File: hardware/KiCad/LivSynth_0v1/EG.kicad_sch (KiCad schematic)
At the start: 28 parts, among them J5 Jumper, Q1 2N3904, Q2 2N3906, Q3 2N3906, Q4 2N3904, SW2 SW_SPST, U1 TL074

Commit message: Initial Routing finished
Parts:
- added D10: LED, LED_THT:LED_D5.0mm, symbol Device:LED
- R10: value 470 -> 360
- RV2, RV3: footprint (none) -> SloBlo:RV141F-40-20BL
- SW2: footprint (none) -> SloBlo:SW_Toggle_MS500C
- U5: renamed from U1; footprint (none) -> Package_SO:SOIC-14_3.9x8.7mm_P1.27mm
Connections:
- net AR_OUT: now also U5.1, U5.2 (-); no longer U5.8, U5.9 (-)
- net at R16.2, R18.1, R23.1: now also U5.5 (+); no longer U5.12 (+)
- net at C32.1, RV2.2, RV2.3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: now also U5.3 (+), U5.6 (-); no longer U5.10 (+), U5.13 (-)
- net at R18.2, SW2.2 (B): now also U5.7; no longer U5.14
- net at D2.2 (A): now also D10.1 (K); no longer R10.2
- net GATE_IN renamed GATE_OUT
- new net: D10.2 (A), R10.2
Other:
- note added: "R = (9-2*1.8)V/.015A = 360R"
- note removed: "R = (9-1.8)V/.015A ~= 470R"
- moved on the sheet: R10
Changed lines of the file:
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@@
+    (stroke (width 0) (type default) (color 0 0 0 0))
+  )
+  (wire (pts (xy 226.695 23.495) (xy 226.695 25.4))
+    (stroke (width 0) (type default) (color 0 0 0 0))
+  )
+  (wire (pts (xy 43.815 134.62) (xy 120.015 134.62))
+    (stroke (width 0) (type default) (color 0 0 0 0))
+  )
+  (wire (pts (xy 169.545 102.87) (xy 169.545 106.045))
+    (stroke (width 0) (type default) (color 0 0 0 0))
+  )
+  (wire (pts (xy 35.56 102.235) (xy 43.815 102.235))
+    (stroke (width 0) (type default) (color 0 0 0 0))
+  )
+  (wire (pts (xy 187.96 87.63) (xy 190.5 87.63))
+    (stroke (width 0) (type default) (color 0 0 0 0))
+  )
+  (wire (pts (xy 207.645 90.17) (xy 205.74 90.17))
+    (stroke (width 0) (type default) (color 0 0 0 0))
+  )
+  (wire (pts (xy 149.225 102.87) (xy 155.575 102.87))
+    (stroke (width 0) (type default) (color 0 0 0 0))
+  )
+  (wire (pts (xy 81.915 95.25) (xy 88.9 95.25))
+    (stroke (width 0) (type default) (color 0 0 0 0))
+  )
+  (wire (pts (xy 187.96 68.58) (xy 187.96 59.055))
+    (stroke (width 0) (type default) (color 0 0 0 0))
+  )
+  (wire (pts (xy 128.27 100.33) (xy 128.27 107.315))
     (stroke (width 0) (type default) (color 0 0 0 0))
   )
@@
     (stroke (width 0) (type default) (color 0 0 0 0))
   )
-  (wire (pts (xy 43.815 134.62) (xy 120.015 134.62))
-    (stroke (width 0) (type default) (color 0 0 0 0))
-  )
-  (wire (pts (xy 169.545 102.87) (xy 169.545 106.045))
-    (stroke (width 0) (type default) (color 0 0 0 0))
-  )
-  (wire (pts (xy 35.56 102.235) (xy 43.815 102.235))
-    (stroke (width 0) (type default) (color 0 0 0 0))
-  )
-  (wire (pts (xy 187.96 87.63) (xy 190.5 87.63))
-    (stroke (width 0) (type default) (color 0 0 0 0))
-  )
-  (wire (pts (xy 207.645 90.17) (xy 205.74 90.17))
-    (stroke (width 0) (type default) (color 0 0 0 0))
-  )
-  (wire (pts (xy 149.225 102.87) (xy 155.575 102.87))
-    (stroke (width 0) (type default) (color 0 0 0 0))
-  )
-  (wire (pts (xy 81.915 95.25) (xy 88.9 95.25))
-    (stroke (width 0) (type default) (color 0 0 0 0))
-  )
-  (wire (pts (xy 187.96 68.58) (xy 187.96 59.055))
-    (stroke (width 0) (type default) (color 0 0 0 0))
-  )
-  (wire (pts (xy 128.27 100.33) (xy 128.27 107.315))
-    (stroke (width 0) (type default) (color 0 0 0 0))
-  )
   (wire (pts (xy 163.195 87.63) (xy 164.465 87.63))
     (stroke (width 0) (type default) (color 0 0 0 0))
@@
     (stroke (width 0) (type default) (color 0 0 0 0))
   )
-  (text "R = (9-1.8)V/.015A ~= 470R" (at 237.49 38.735 0)
+  (text "R = (9-2*1.8)V/.015A = 360R" (at 237.49 38.735 0)
     (effects (font (size 1.27 1.27)) (justify left bottom))
   )
@@
     (effects (font (size 1.27 1.27)) (justify left bottom))
   )
-  (hierarchical_label "GATE_IN" (shape input) (at 26.035 102.235 180)
+  (hierarchical_label "GATE_OUT" (shape input) (at 26.035 102.235 180)
     (effects (font (size 1.27 1.27)) (justify right))
   )
@@
     (pin "1")
   )
-  (symbol (lib_id "Amplifier_Operational:TL074") (at 198.12 90.17 0) (mirror x) (unit 4)
+  (symbol (lib_id "Amplifier_Operational:TL074") (at 198.12 90.17 0) (mirror x) (unit 2)
     (in_bom yes) (on_board yes)
-    (property "Reference" "U1" (id 0) (at 198.12 82.55 0))
+    (property "Reference" "U5" (id 0) (at 198.12 82.55 0))
     (property "Value" "TL074" (id 1) (at 198.12 84.455 0))
-    (property "Footprint" "" (id 2) (at 196.85 92.71 0)
+    (property "Footprint" "Package_SO:SOIC-14_3.9x8.7mm_P1.27mm" (id 2) (at 196.85 92.71 0)
       (effects (font (size 1.27 1.27)) hide)
     )
@@
     (pin "2")
   )
-  (symbol (lib_id "Amplifier_Operational:TL074") (at 198.12 71.12 0) (mirror x) (unit 3)
+  (symbol (lib_id "Amplifier_Operational:TL074") (at 198.12 71.12 0) (mirror x) (unit 1)
     (in_bom yes) (on_board yes)
-    (property "Reference" "U1" (id 0) (at 198.12 63.5 0))
+    (property "Reference" "U5" (id 0) (at 198.12 63.5 0))
     (property "Value" "TL074" (id 1) (at 198.12 65.405 0))
-    (property "Footprint" "" (id 2) (at 196.85 73.66 0)
+    (property "Footprint" "Package_SO:SOIC-14_3.9x8.7mm_P1.27mm" (id 2) (at 196.85 73.66 0)
       (effects (font (size 1.27 1.27)) hide)
     )
@@
     (property "Reference" "RV2" (id 0) (at 159.385 90.805 90))
     (property "Value" "1M" (id 1) (at 159.385 93.345 90))
-    (property "Footprint" "" (id 2) (at 159.385 87.63 0)
+    (property "Footprint" "SloBlo:RV141F-40-20BL" (id 2) (at 159.385 87.63 0)
       (effects (font (size 1.27 1.27)) hide)
     )
@@
     (pin "1")
   )
+  (symbol (lib_id "Device:LED") (at 226.695 38.735 90) (unit 1)
+    (in_bom yes) (on_board yes) (fields_autoplaced)
+    (property "Reference" "D10" (id 0) (at 230.505 39.0524 90)
+      (effects (font (size 1.27 1.27)) (justify right))
+    )
+    (property "Value" "LED" (id 1) (at 230.505 41.5924 90)
+      (effects (font (size 1.27 1.27)) (justify right))
+    )
+    (property "Footprint" "LED_THT:LED_D5.0mm" (id 2) (at 226.695 38.735 0)
+      (effects (font (size 1.27 1.27)) hide)
+    )
+    (property "Datasheet" "~" (id 3) (at 226.695 38.735 0)
+      (effects (font (size 1.27 1.27)) hide)
+    )
+    (pin "1")
+    (pin "2")
+  )
   (symbol (lib_id "power:GND") (at 81.915 118.11 0) (unit 1)
     (in_bom yes) (on_board yes) (fields_autoplaced)
@@
     (pin "1")
   )
-  (symbol (lib_id "power:+9V") (at 226.695 33.02 0) (unit 1)
-    (in_bom yes) (on_board yes) (fields_autoplaced)
-    (property "Reference" "#PWR032" (id 0) (at 226.695 36.83 0)
-      (effects (font (size 1.27 1.27)) hide)
-    )
-    (property "Value" "+9V" (id 1) (at 226.695 27.305 0))
-    (property "Footprint" "" (id 2) (at 226.695 33.02 0)
-      (effects (font (size 1.27 1.27)) hide)
-    )
-    (property "Datasheet" "" (id 3) (at 226.695 33.02 0)
+  (symbol (lib_id "power:+9V") (at 226.695 23.495 0) (unit 1)
+    (in_bom yes) (on_board yes) (fields_autoplaced)
+    (property "Reference" "#PWR032" (id 0) (at 226.695 27.305 0)
+      (effects (font (size 1.27 1.27)) hide)
+    )
+    (property "Value" "+9V" (id 1) (at 226.695 17.78 0))
+    (property "Footprint" "" (id 2) (at 226.695 23.495 0)
+      (effects (font (size 1.27 1.27)) hide)
+    )
+    (property "Datasheet" "" (id 3) (at 226.695 23.495 0)
       (effects (font (size 1.27 1.27)) hide)
     )
@@
     (property "Reference" "RV3" (id 0) (at 159.385 106.045 90))
     (property "Value" "1M" (id 1) (at 159.385 108.585 90))
-    (property "Footprint" "" (id 2) (at 159.385 102.87 0)
+    (property "Footprint" "SloBlo:RV141F-40-20BL" (id 2) (at 159.385 102.87 0)
       (effects (font (size 1.27 1.27)) hide)
     )
@@
     (property "Reference" "SW2" (id 0) (at 125.095 128.27 0))
     (property "Value" "SW_SPST" (id 1) (at 125.095 130.81 0))
-    (property "Footprint" "" (id 2) (at 125.095 134.62 0)
+    (property "Footprint" "SloBlo:SW_Toggle_MS500C" (id 2) (at 125.095 134.62 0)
       (effects (font (size 1.27 1.27)) hide)
     )
@@
     (pin "2")
   )
-  (symbol (lib_id "Device:R") (at 226.695 38.735 0) (unit 1)
-    (in_bom yes) (on_board yes) (fields_autoplaced)
-    (property "Reference" "R10" (id 0) (at 228.6 37.4649 0)
-      (effects (font (size 1.27 1.27)) (justify left))
-    )
-    (property "Value" "470" (id 1) (at 228.6 40.0049 0)
-      (effects (font (size 1.27 1.27)) (justify left))
-    )
-    (property "Footprint" "Resistor_THT:R_Axial_DIN0207_L6.3mm_D2.5mm_P7.62mm_Horizontal" (id 2) (at 224.917 38.735 90)
-      (effects (font (size 1.27 1.27)) hide)
-    )
-    (property "Datasheet" "~" (id 3) (at 226.695 38.735 0)
-      (effects (font (size 1.27 1.27)) hide)
-    )
+  (symbol (lib_id "Device:R") (at 226.695 29.21 0) (unit 1)
+    (in_bom yes) (on_board yes) (fields_autoplaced)
+    (property "Reference" "R10" (id 0) (at 228.6 27.9399 0)
+      (effects (font (size 1.27 1.27)) (justify left))
+    )
+    (property "Value" "360" (id 1) (at 228.6 30.4799 0)
+      (effects (font (size 1.27 1.27)) (justify left))
+    )
+    (property "Footprint" "Resistor_THT:R_Axial_DIN0207_L6.3mm_D2.5mm_P7.62mm_Horizontal" (id 2) (at 224.917 29.21 90)
+      (effects (font (size 1.27 1.27)) hide)
+    )
+    (property "Datasheet" "~" (id 3) (at 226.695 29.21 0)
+      (effects (font (size 1.27 1.27)) hide)
+    )

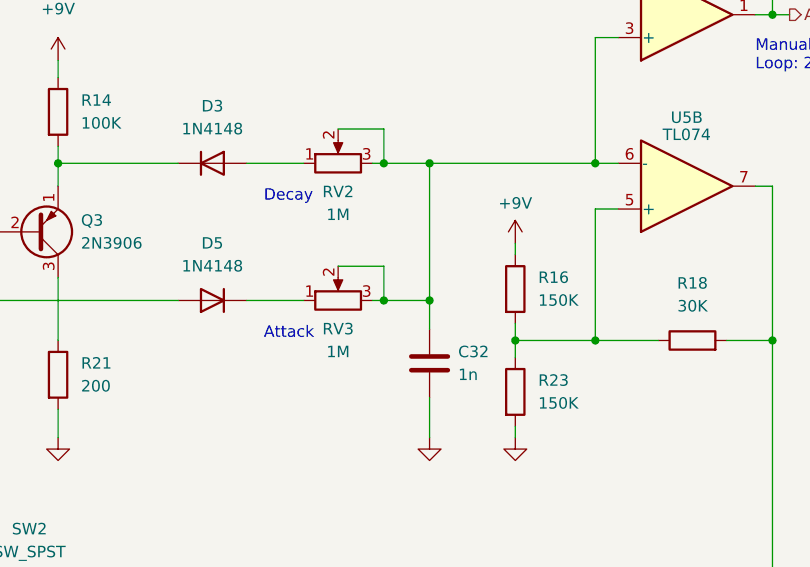
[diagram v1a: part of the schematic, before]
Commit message: Rework for polyester film capacitors
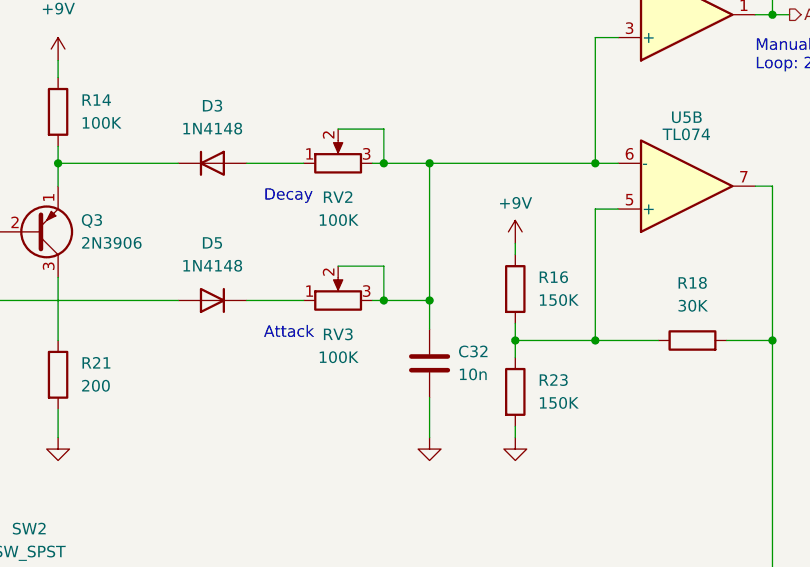
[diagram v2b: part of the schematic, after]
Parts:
- C32: value 1n -> 10n; footprint Capacitor_THT:C_Disc_D3.0mm_W1.6mm_P2.50mm -> Capacitor_THT:C_Rect_L7.2mm_W2.5mm_P5.00mm_FKS2_FKP2_MKS2_MKP2
- RV2, RV3: value 1M -> 100K
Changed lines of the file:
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@@
   (symbol (lib_id "Device:R_Potentiometer") (at 159.385 87.63 90) (unit 1)
     (in_bom yes) (on_board yes) (fields_autoplaced)
-    (property "Reference" "RV2" (id 0) (at 159.385 90.805 90))
-    (property "Value" "1M" (id 1) (at 159.385 93.345 90))
+    (property "Reference" "RV2" (id 0) (at 159.385 91.44 90))
+    (property "Value" "100K" (id 1) (at 159.385 93.98 90))
     (property "Footprint" "SloBlo:RV141F-40-20BL" (id 2) (at 159.385 87.63 0)
       (effects (font (size 1.27 1.27)) hide)
@@
       (effects (font (size 1.27 1.27)) (justify left))
     )
-    (property "Value" "1n" (id 1) (at 172.72 111.1249 0)
-      (effects (font (size 1.27 1.27)) (justify left))
-    )
-    (property "Footprint" "Capacitor_THT:C_Disc_D3.0mm_W1.6mm_P2.50mm" (id 2) (at 170.5102 113.665 0)
+    (property "Value" "10n" (id 1) (at 172.72 111.1249 0)
+      (effects (font (size 1.27 1.27)) (justify left))
+    )
+    (property "Footprint" "Capacitor_THT:C_Rect_L7.2mm_W2.5mm_P5.00mm_FKS2_FKP2_MKS2_MKP2" (id 2) (at 170.5102 113.665 0)
       (effects (font (size 1.27 1.27)) hide)
     )
@@
   (symbol (lib_id "Device:R_Potentiometer") (at 159.385 102.87 90) (unit 1)
     (in_bom yes) (on_board yes) (fields_autoplaced)
-    (property "Reference" "RV3" (id 0) (at 159.385 106.045 90))
-    (property "Value" "1M" (id 1) (at 159.385 108.585 90))
+    (property "Reference" "RV3" (id 0) (at 159.385 106.68 90))
+    (property "Value" "100K" (id 1) (at 159.385 109.22 90))
     (property "Footprint" "SloBlo:RV141F-40-20BL" (id 2) (at 159.385 102.87 0)
       (effects (font (size 1.27 1.27)) hide)

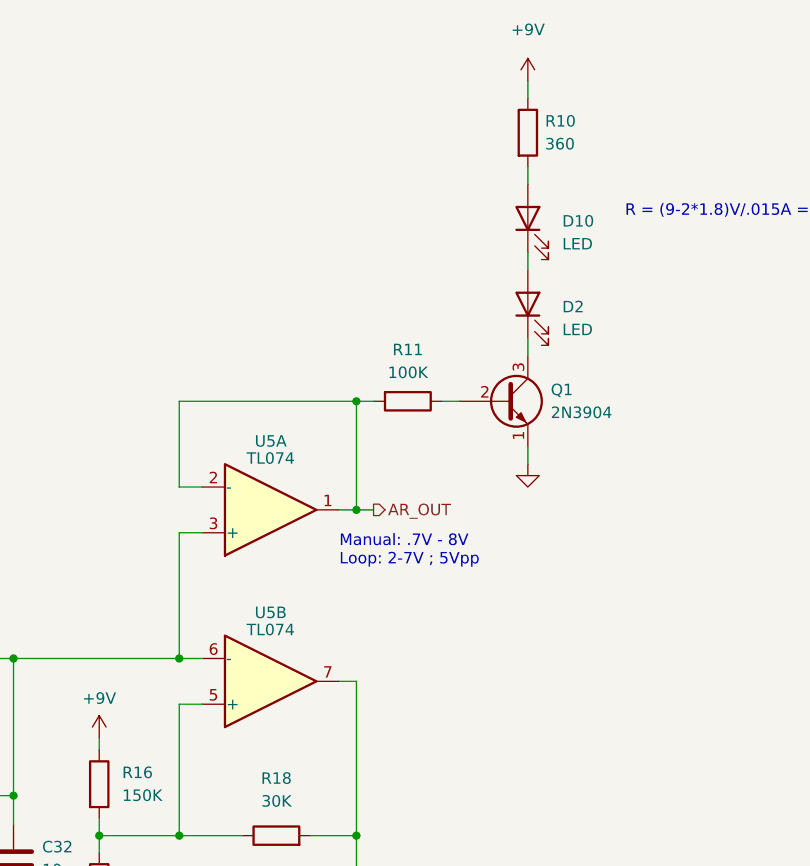
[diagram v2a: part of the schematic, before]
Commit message: Change LED status circuits
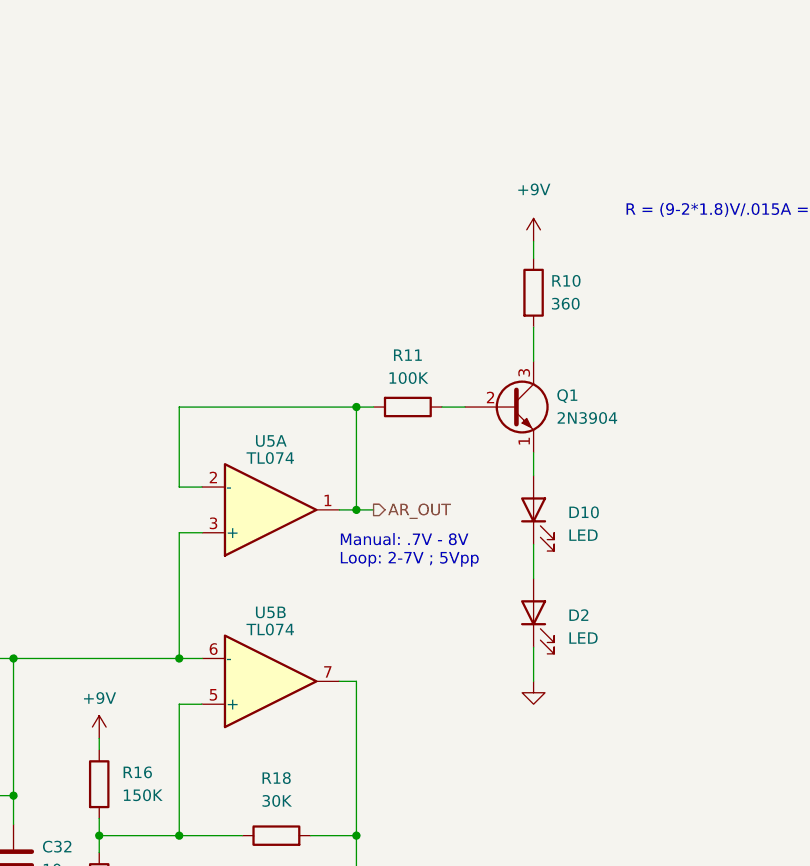
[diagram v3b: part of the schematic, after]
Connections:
- net GND: now also D2.1 (K); no longer Q1.1 (E)
- net at Q1.3 (C): now also R10.2; no longer D2.1 (K)
- net at D10.2 (A): now also Q1.1 (E); no longer R10.2
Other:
- moved on the sheet: D10, D2, Q1, R10, R11

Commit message: 0v1 Ready for Production
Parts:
- renumbered C32 to C26, D5 to D11, D10 to D3, D4 to D7, D3 to D8, D2 to D9, J5 to J7, Q3 to Q11, Q1 to Q2, Q4 to Q7, Q2 to Q8, R15 to R21, R12 to R23, R19 to R24, R11 to R27, R14 to R42, R21 to R43, R13 to R45, R20 to R46, R10 to R6, R16 to R69, R17 to R7, R23 to R70, R22 to R72, R18 to R73, RV3 to RV4, RV2 to RV8, U5 to U6
